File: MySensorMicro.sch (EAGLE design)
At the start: 23 parts, among them IC1 MEGA328P-AU, IC2 AT25DF512C-SSHN-B, IC3 SI7021, IC4 ATSHA204A, Q1 N/M

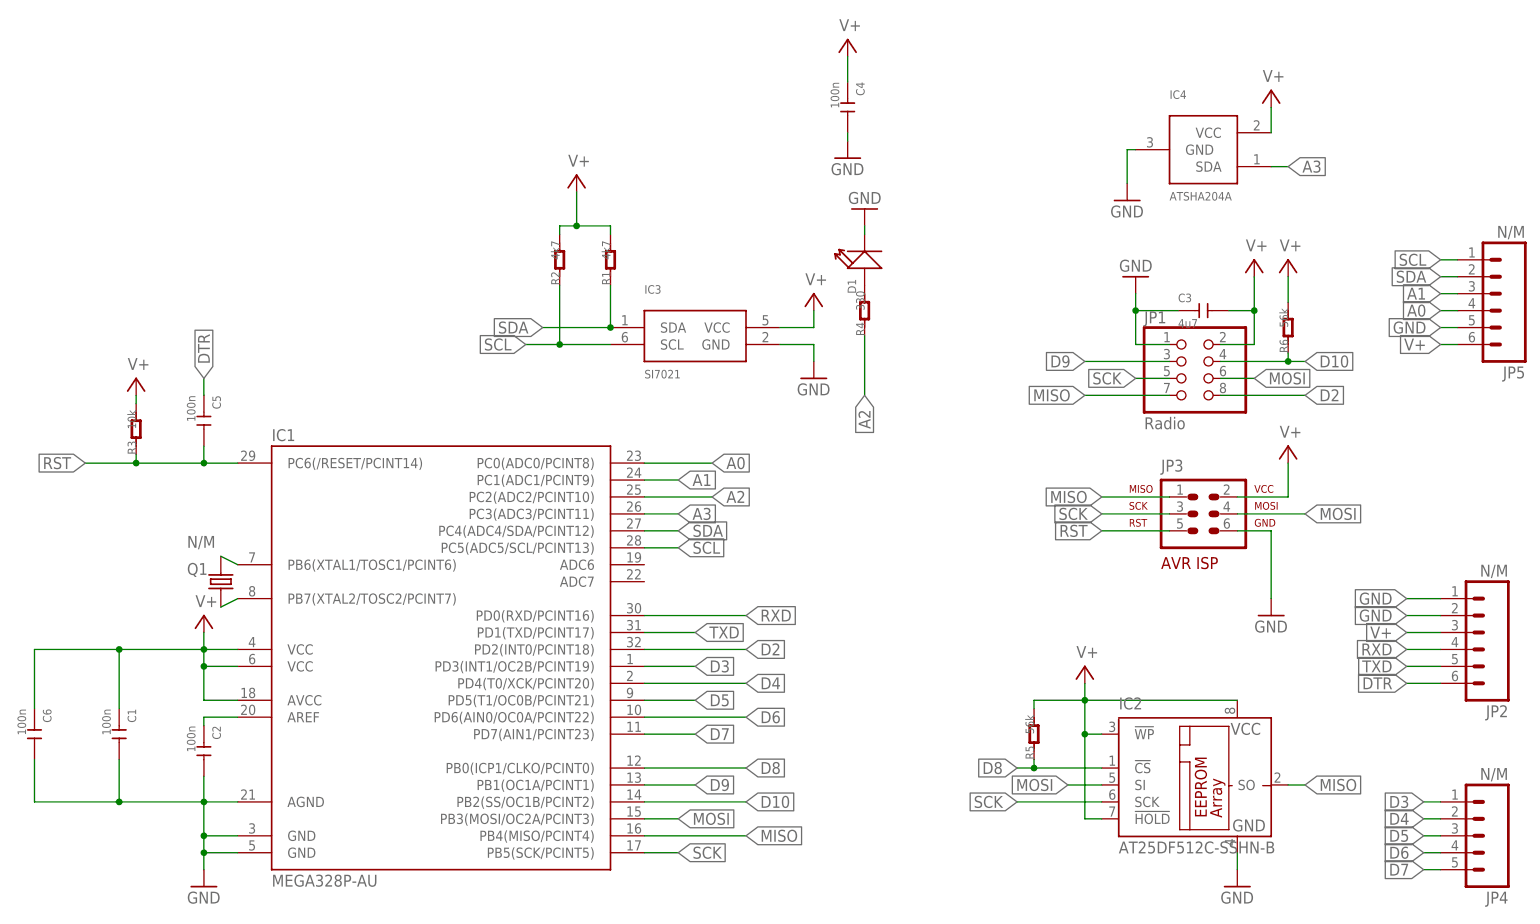
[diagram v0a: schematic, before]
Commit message: Change passive components in schematic to 0603 package
This initial branch includes changes in the following:
- schematic layout: change passive components to 0603 package.
- board layout: NOT yet in the correct position as the new package size
caused overlaps with other components. This will be fixed in next
releases.
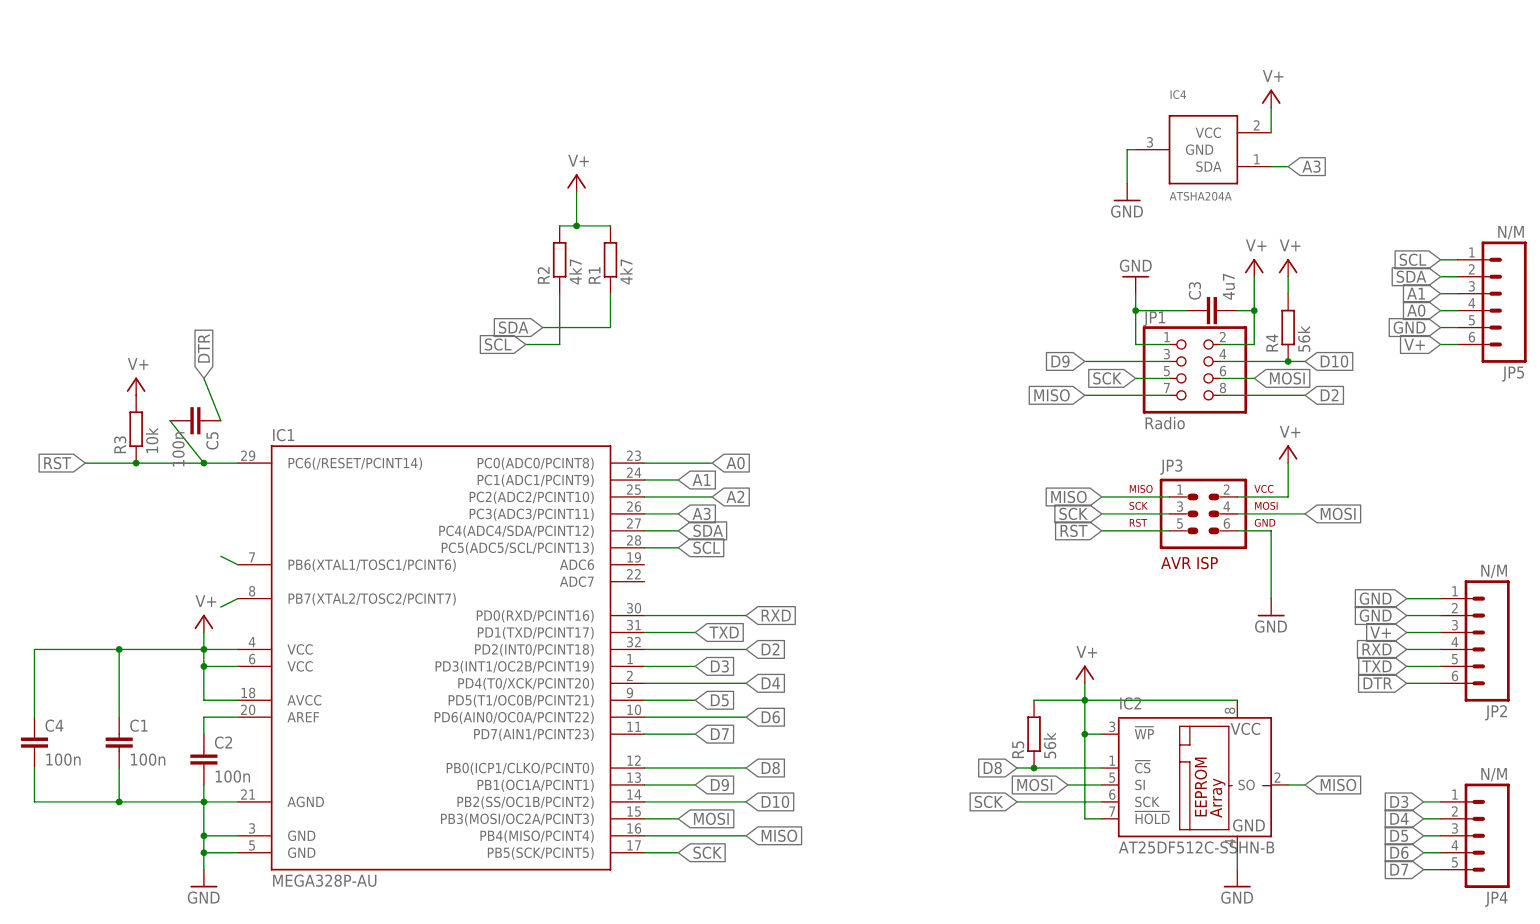
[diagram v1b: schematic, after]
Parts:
- removed C6: 100n, Discrete:CAP-0402
- removed D1: (no value), Discrete:LED-0402
- removed IC3: SI7021, Sensor:SI7021
- removed Q1: N/M, Discrete:CRYSTAL-306010055
- removed R6: 56k, Discrete:R-0402
- C1, C2, C4, C5: device Discrete:CAP-0402 -> resistor:C-EUC0603K
- C3: device Discrete:CAP-0603 -> resistor:C-EUC0603K
- R1, R2, R3, R5: device Discrete:R-0402 -> resistor:R-EU_R0603
- R4: value 330 -> 56k; device Discrete:R-0402 -> resistor:R-EU_R0603
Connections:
- removed net N$3: D1.+, R4.2
- net A2: no longer R4.1
- net D10: now also R4.1; no longer R6.1
- net GND: no longer C6.2, D1.-, IC3.GND
- net N$1: no longer Q1.1
- net N$2: no longer Q1.2
- net SCL: no longer IC3.SCL
- net SDA: no longer IC3.SDA
- net V+: now also R4.2; no longer C6.1, IC3.VCC, R6.2

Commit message: Adapt PCB layout to 0603 package size "major change"
* Schematic
- rotate C5
- delete X1 "crystal"

* PCB Layout "major change"

- Change board size to 19.5x17.5
- All passive componets are changed to 0603 package size
- Delete SI7021 sensor
- Delete C4 and renumbering capacitors' numbers
- Delete R4 and renumbering resisots' numbers
- Delete D1
- Delete Q1 crystal

* Full re-arrangment of passive componets to fit the new 0603

- Moved C4, R3 to button layer
- All other passive componets have been reoriented
- Moved the eeprom chip a few milli meters above so that R4 can fit

** This version has been checked for DRC
** This version will be reviewed again ana make sure all pins are
connected correctly and nothing is missing
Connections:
- removed net N$1: IC1.PB6(XTAL1/TOSC1/PCINT6)
- removed net N$2: IC1.PB7(XTAL2/TOSC2/PCINT7)
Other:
- moved on the sheet: C5
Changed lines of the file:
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@@
 <instance part="SUPPLY8" gate="1" x="78.74" y="121.92"/>
 <instance part="JP2" gate="G$1" x="213.36" y="53.34" rot="R180"/>
-<instance part="C5" gate="G$1" x="22.86" y="85.09" rot="R270"/>
+<instance part="C5" gate="G$1" x="22.86" y="85.09"/>
 <instance part="JP4" gate="G$1" x="215.9" y="22.86" rot="R180"/>
 <instance part="JP5" gate="G$1" x="215.9" y="104.14" rot="R180"/>
@@
 <pinref part="IC1" gate="1" pin="PC6(/RESET/PCINT14)"/>
 <wire x1="22.86" y1="78.74" x2="27.94" y2="78.74" width="0.1524" layer="91"/>
-<wire x1="17.78" y1="85.09" x2="22.86" y2="78.74" width="0.1524" layer="91"/>
+<wire x1="22.86" y1="80.01" x2="22.86" y2="78.74" width="0.1524" layer="91"/>
 <junction x="22.86" y="78.74"/>
 <wire x1="5.08" y1="78.74" x2="12.7" y2="78.74" width="0.1524" layer="91"/>
@@
 </segment>
 </net>
-<net name="N$1" class="0">
-<segment>
-<pinref part="IC1" gate="1" pin="PB6(XTAL1/TOSC1/PCINT6)"/>
-<wire x1="25.4" y1="64.77" x2="27.94" y2="63.5" width="0.1524" layer="91"/>
-</segment>
-</net>
-<net name="N$2" class="0">
-<segment>
-<pinref part="IC1" gate="1" pin="PB7(XTAL2/TOSC2/PCINT7)"/>
-<wire x1="27.94" y1="58.42" x2="25.4" y2="57.15" width="0.1524" layer="91"/>
-</segment>
-</net>
 <net name="DTR" class="0">
 <segment>
@@
 <segment>
 <pinref part="C5" gate="G$1" pin="1"/>
-<wire x1="25.4" y1="85.09" x2="22.86" y2="91.44" width="0.1524" layer="91"/>
+<wire x1="22.86" y1="87.63" x2="22.86" y2="91.44" width="0.1524" layer="91"/>
 <label x="22.86" y="91.44" size="1.778" layer="95" rot="R90" xref="yes"/>
 </segment>
